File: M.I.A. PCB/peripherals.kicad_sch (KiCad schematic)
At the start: 59 parts, among them J10 Conn_01x03, J11 Conn_01x03, J12 Screw_Terminal_01x02, J13 Screw_Terminal_01x02, J15 Screw_Terminal_01x02, J16 Screw_Terminal_01x02, J17 Screw_Terminal_01x02, J19 Conn_01x08_Socket, J20 Screw_Terminal_01x02, J21 Conn_01x04_Socket, J22 Conn_01x04_Socket, J23 Conn_01x04_Socket, J24 Conn_01x04_Socket, J3 Conn_01x03, J4 Conn_01x03, J5 Conn_01x03, J6 Conn_01x03, J7 MSD-4-A, J8 Conn_01x03, J9 Conn_01x03, Q1 AO3400A, Q2 AO3400A, Q3 AO3400A, Q4 AO3400A, U15 74AHC541

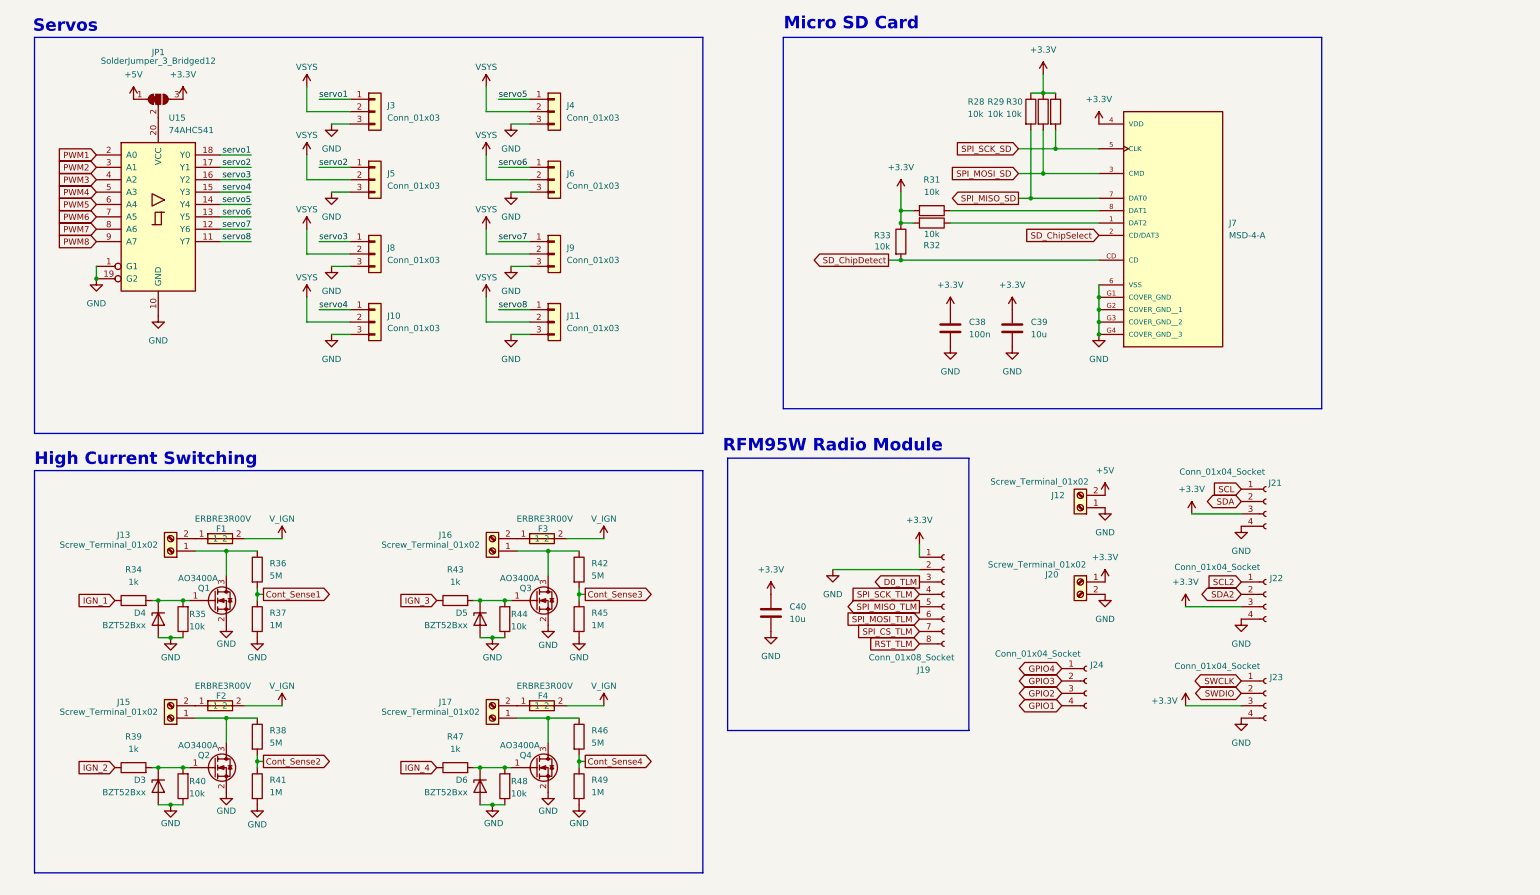
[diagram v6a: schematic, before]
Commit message: Routed GPS Maybe Correctly
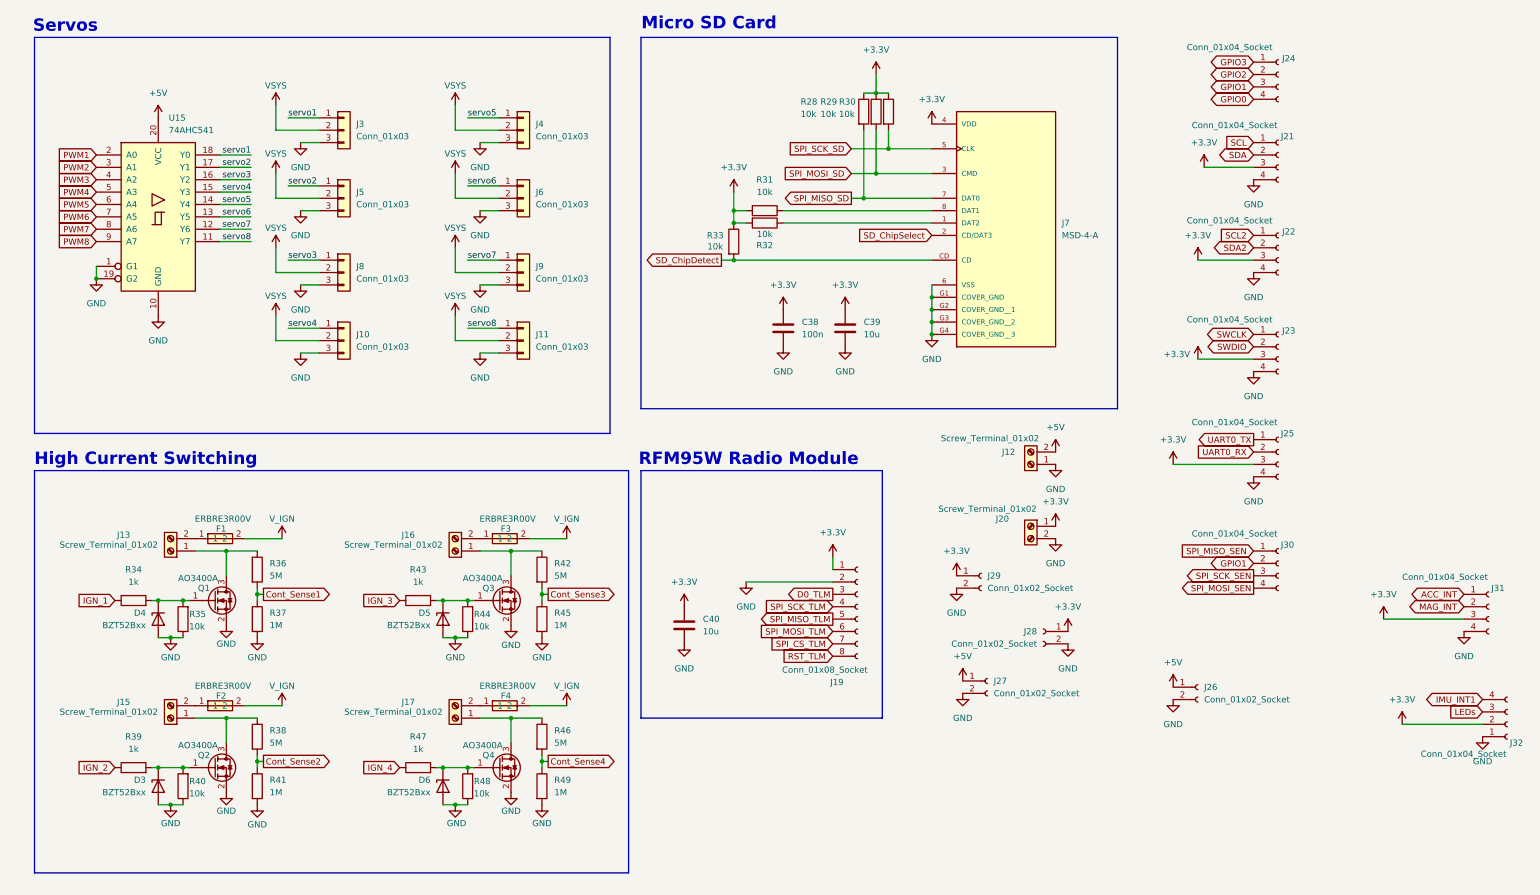
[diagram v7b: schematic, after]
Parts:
- removed JP1: SolderJumper_3_Bridged12, Jumper:SolderJumper-3_P1.3mm_Bridged12_RoundedPad1.0x1.5mm, symbol Jumper:SolderJumper_3_Bridged12
- added J25, J30, J31, J32: Conn_01x04_Socket, Connector_JST:JST_PH_B4B-PH-K_1x04_P2.00mm_Vertical, symbol Connector:Conn_01x04_Socket
- added J26, J27, J28, J29: Conn_01x02_Socket, Connector_JST:JST_PH_B2B-PH-K_1x02_P2.00mm_Vertical, symbol Connector:Conn_01x02_Socket
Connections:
- net GPIO4 is gone; now on net GPIO3: J24.1 (Pin_1)
- net +3.3V: now also J25.3 (Pin_3), J28.1 (Pin_1), J29.1 (Pin_1), J31.3 (Pin_3), J32.2 (Pin_2)
- net +5V: now also U15.20 (VCC), J26.1 (Pin_1), J27.1 (Pin_1)
- net GND: now also J25.4 (Pin_4), J26.2 (Pin_2), J27.2 (Pin_2), J28.2 (Pin_2), J29.2 (Pin_2), J31.4 (Pin_4), J32.1 (Pin_1)
- net GPIO1: now also J24.3 (Pin_3), J30.2 (Pin_2); no longer J24.4 (Pin_4)
- net GPIO2: now also J24.2 (Pin_2); no longer J24.3 (Pin_3)
- net GPIO3: no longer J24.2 (Pin_2)
- new net ACC_INT: J31.1 (Pin_1)
- new net GPIO0: J24.4 (Pin_4)
- new net IMU_INT1: J32.4 (Pin_4)
- new net LEDs: J32.3 (Pin_3)
- new net MAG_INT: J31.2 (Pin_2)
- new net SPI_MISO_SEN: J30.1 (Pin_1)
- new net SPI_MOSI_SEN: J30.4 (Pin_4)
- new net SPI_SCK_SEN: J30.3 (Pin_3)
- new net UART0_RX: J25.2 (Pin_2)
- new net UART0_TX: J25.1 (Pin_1)
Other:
- moved on the sheet: C38, C39, C40, D5, D6, F3, F4, J10, J11, J12, J16, J17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

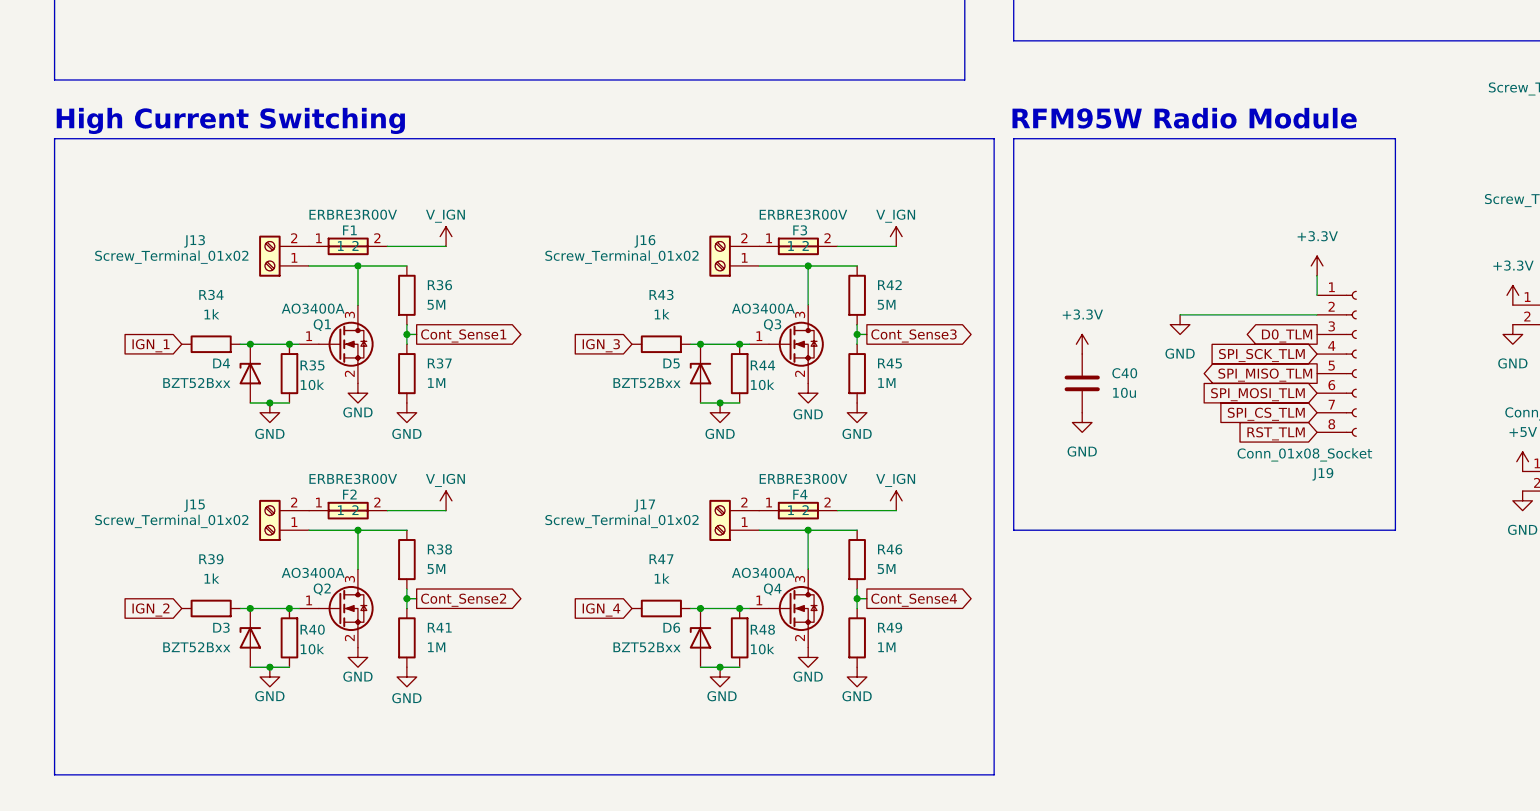
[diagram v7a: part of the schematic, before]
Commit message: Added LEDs, Prepped for 4 layer conversion
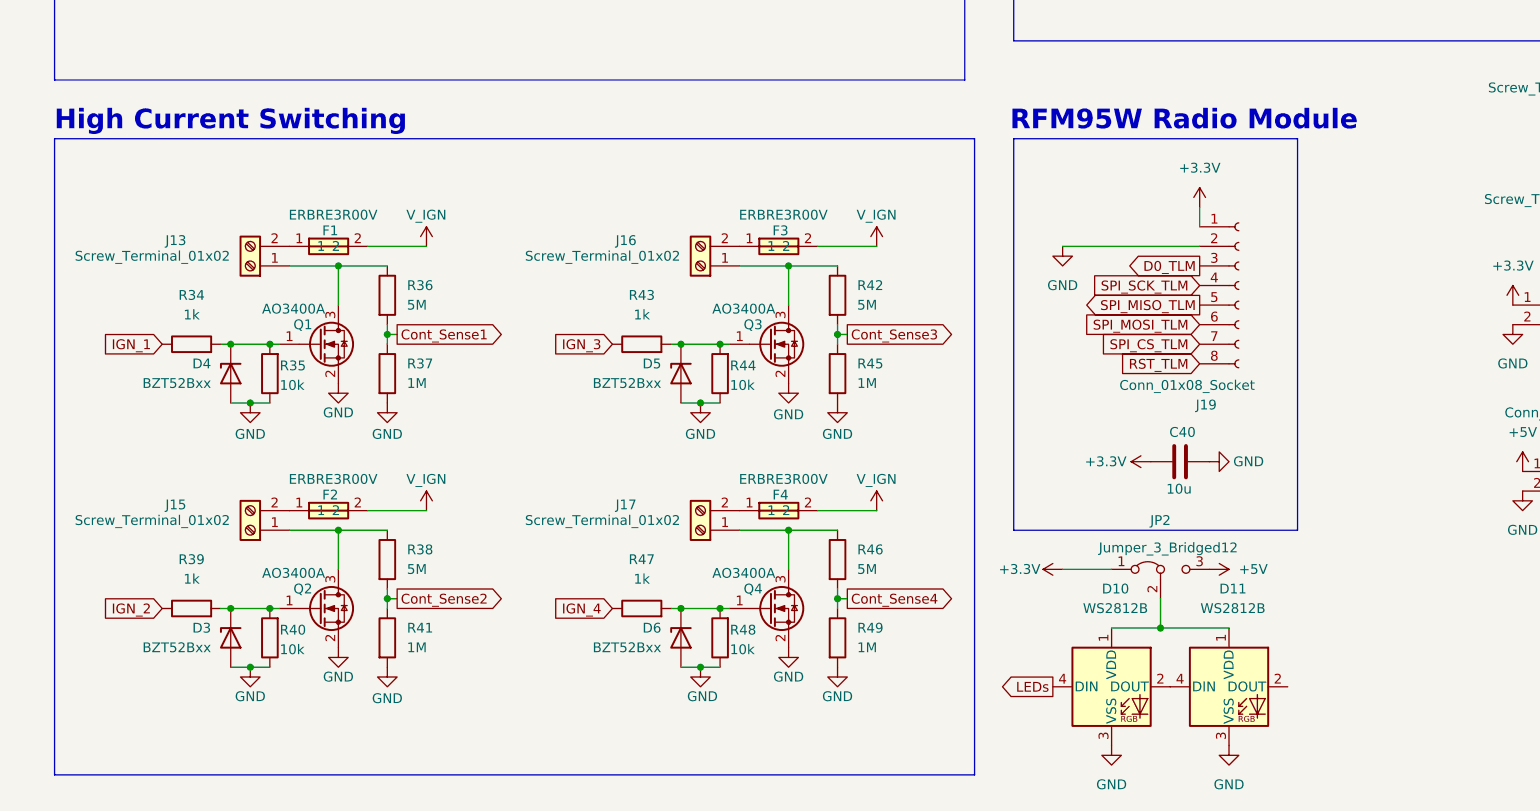
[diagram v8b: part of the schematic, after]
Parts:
- added D10, D11: WS2812B, LED_SMD:LED_WS2812B_PLCC4_5.0x5.0mm_P3.2mm, symbol LED:WS2812B
- added JP2: Jumper_3_Bridged12, Jumper:SolderJumper-3_P1.3mm_Bridged12_RoundedPad1.0x1.5mm_NumberLabels, symbol Jumper:Jumper_3_Bridged12
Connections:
- net +3.3V: now also JP2.1 (A)
- net +5V: now also JP2.3 (B)
- net GND: now also D10.3 (VSS), D11.3 (VSS)
- net LEDs: now also D10.4 (DIN)
- new net: D10.1 (VDD), D11.1 (VDD), JP2.2 (C)
- new net: D10.2 (DOUT), D11.4 (DIN)
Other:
- moved on the sheet: C40, D3, D4, D5, D6, F1, F2, F3, F4, J13, J15, J16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
